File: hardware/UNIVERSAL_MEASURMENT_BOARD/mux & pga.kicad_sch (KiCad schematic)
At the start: 11 parts, among them U3 PGA280AIPW, U4 CD4097BM

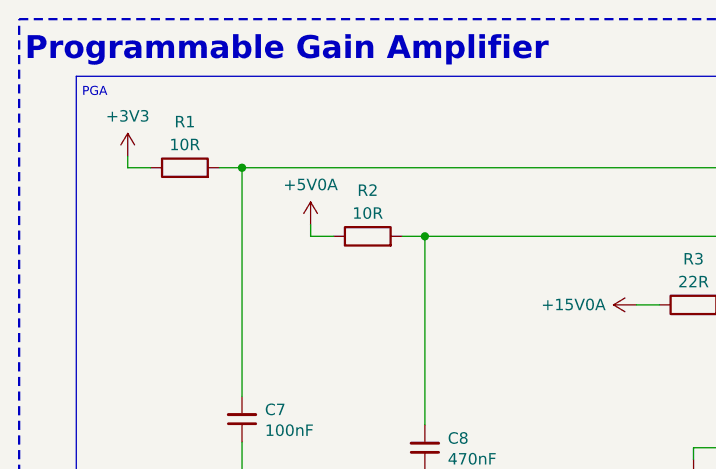
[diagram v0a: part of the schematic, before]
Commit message: Fixed VOUT range of PGA to 3.0V, fixed GPIO connection between FDCAN and MCU, added 1.5V VREF to PGA, changed value of enable divider of 7V DCDC converter.
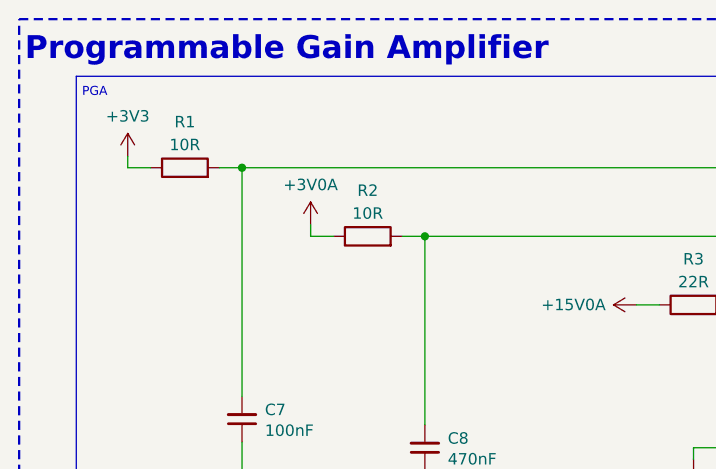
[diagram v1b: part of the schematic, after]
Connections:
- net +5V0A renamed +3V0A
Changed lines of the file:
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@@
 (kicad_sch
-	(version 20260101)
+	(version 20260306)
 	(generator "eeschema")
 	(generator_version "10.0")
@@
 		(title "Universal Measurment Board")
 		(date "2026-03-26")
-		(rev "1.9.21")
+		(rev "1.11.22")
 		(company "PUT Motorsport Formula Student Team")
 		(comment 1 "Designed by Marcin Trzmiel under")
@@
 			)
 		)
-		(property "Value" "+5V0A"
+		(property "Value" "+3V0A"
 			(at 53.975 40.005 0)
 			(show_name no)

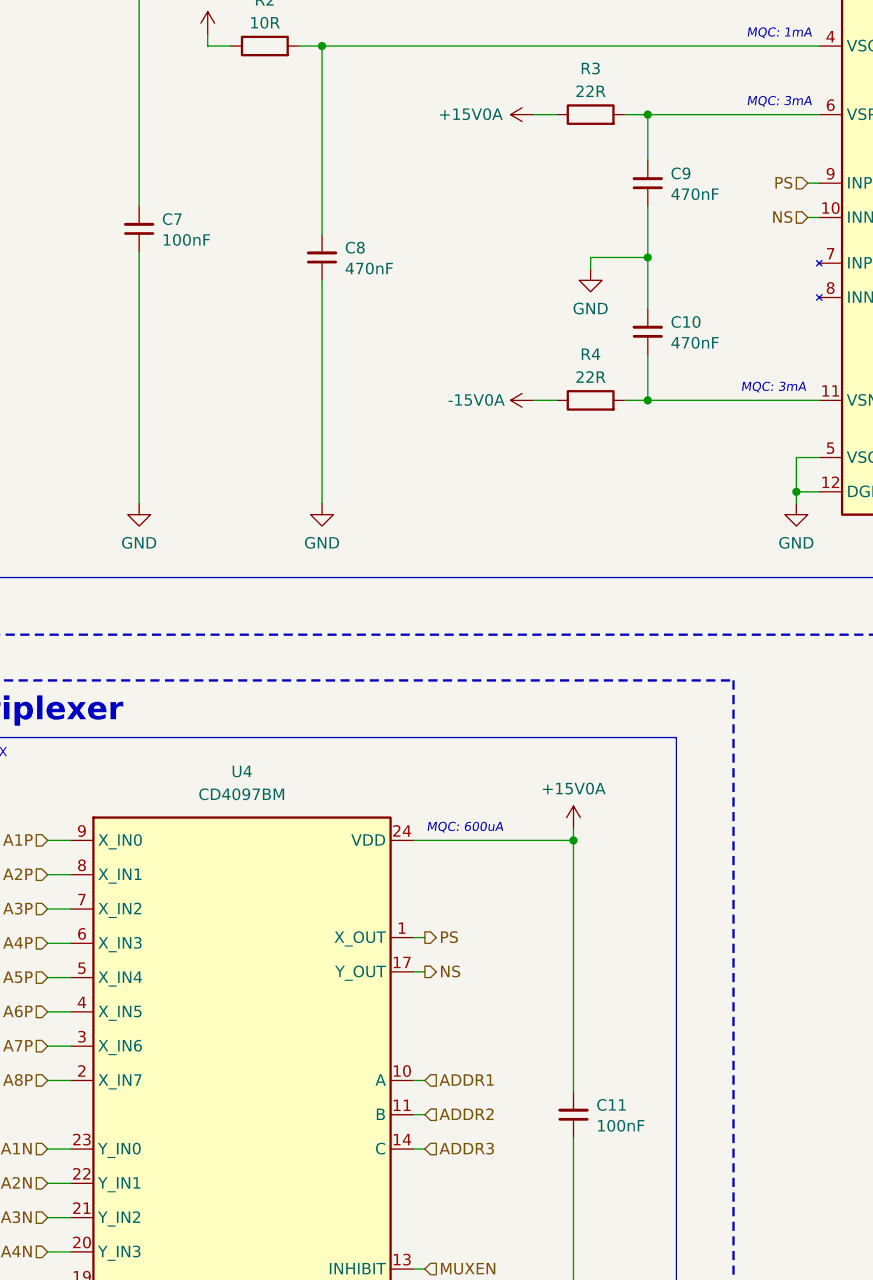
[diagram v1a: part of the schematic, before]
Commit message: Reduced PCB dimensions, working on power section
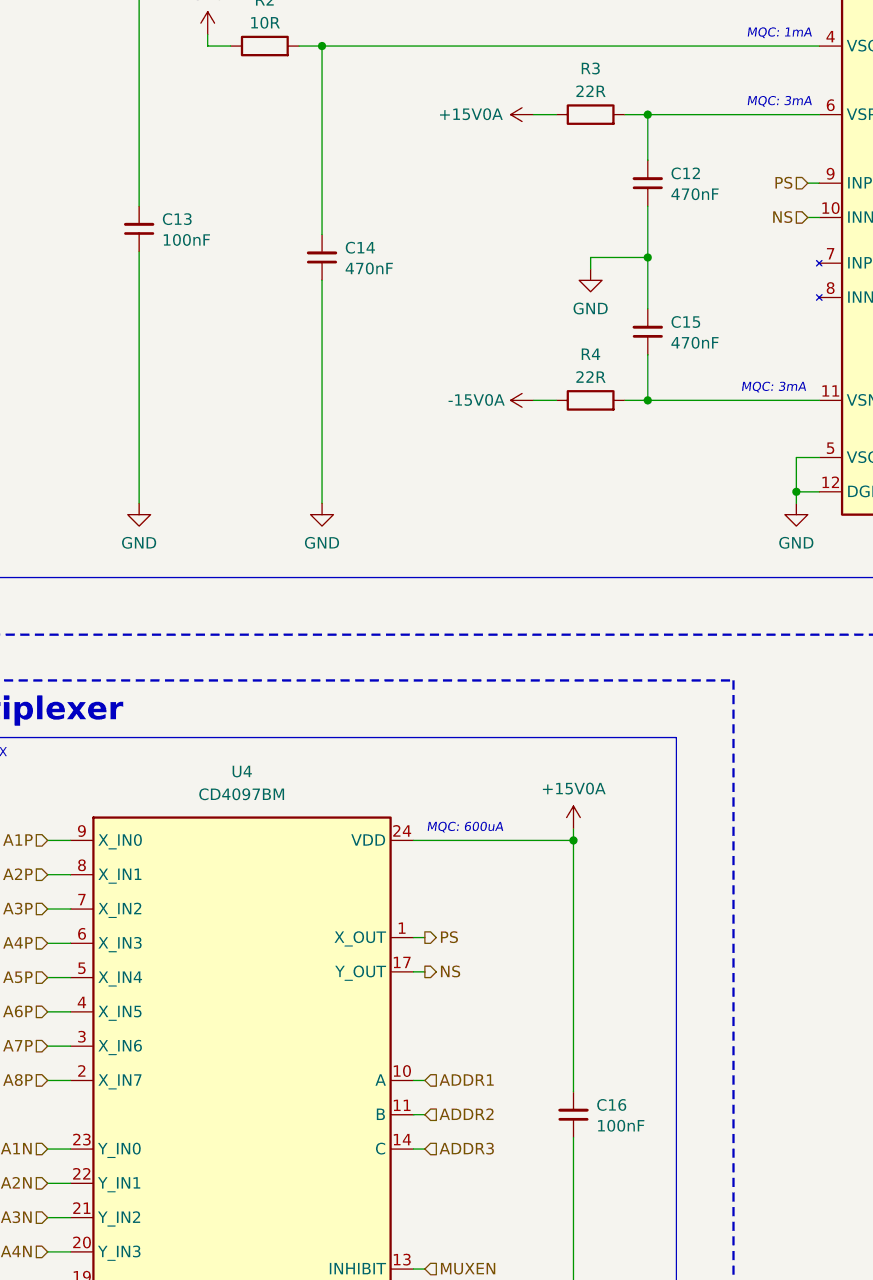
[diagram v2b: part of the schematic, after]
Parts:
- renumbered C9 to C12, C7 to C13, C8 to C14, C10 to C15, C11 to C16
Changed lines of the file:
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@@
 		(in_pos_files yes)
 		(dnp no)
-		(property "Reference" "#PWR024"
+		(property "Reference" "#PWR031"
 			(at 96.52 76.835 0)
 			(hide yes)
@@
 			(project "UNIVERSAL_MEASURMENT_BOARD"
 				(path "/92c00310-4384-4ef3-9368-efad75526047/2f9d6be2-539e-4cd2-829d-3839cc14b053"
-					(reference "#PWR024")
+					(reference "#PWR031")
 					(unit 1)
 				)
@@
 		(in_pos_files yes)
 		(dnp no)
-		(property "Reference" "#PWR022"
+		(property "Reference" "#PWR030"
 			(at 93.98 53.34 0)
 			(hide yes)
@@
 			(project "UNIVERSAL_MEASURMENT_BOARD"
 				(path "/92c00310-4384-4ef3-9368-efad75526047/2f9d6be2-539e-4cd2-829d-3839cc14b053"
-					(reference "#PWR022")
+					(reference "#PWR030")
 					(unit 1)
 				)
@@
 		(in_pos_files yes)
 		(dnp no)
-		(property "Reference" "C10"
+		(property "Reference" "C15"
 			(at 105.41 76.4286 0)
 			(show_name no)
@@
 			(project "UNIVERSAL_MEASURMENT_BOARD"
 				(path "/92c00310-4384-4ef3-9368-efad75526047/2f9d6be2-539e-4cd2-829d-3839cc14b053"
-					(reference "C10")
+					(reference "C15")
 					(unit 1)
 				)
@@
 		(in_pos_files yes)
 		(dnp no)
-		(property "Reference" "C8"
+		(property "Reference" "C14"
 			(at 69.215 68.1736 0)
 			(show_name no)
@@
 			(project "UNIVERSAL_MEASURMENT_BOARD"
 				(path "/92c00310-4384-4ef3-9368-efad75526047/2f9d6be2-539e-4cd2-829d-3839cc14b053"
-					(reference "C8")
+					(reference "C14")
 					(unit 1)
 				)
@@
 		(in_pos_files yes)
 		(dnp no)
-		(property "Reference" "#PWR021"
+		(property "Reference" "#PWR034"
 			(at 66.675 102.87 0)
 			(hide yes)
@@
 			(project "UNIVERSAL_MEASURMENT_BOARD"
 				(path "/92c00310-4384-4ef3-9368-efad75526047/2f9d6be2-539e-4cd2-829d-3839cc14b053"
-					(reference "#PWR021")
+					(reference "#PWR034")
 					(unit 1)
 				)
@@
 		(in_pos_files yes)
 		(dnp no)
-		(property "Reference" "#PWR029"
+		(property "Reference" "#PWR038"
 			(at 94.615 202.565 0)
 			(hide yes)
@@
 			(project "UNIVERSAL_MEASURMENT_BOARD"
 				(path "/92c00310-4384-4ef3-9368-efad75526047/2f9d6be2-539e-4cd2-829d-3839cc14b053"
-					(reference "#PWR029")
+					(reference "#PWR038")
 					(unit 1)
 				)
@@
 		(in_pos_files yes)
 		(dnp no)
-		(property "Reference" "#PWR028"
+		(property "Reference" "#PWR036"
 			(at 94.615 136.525 0)
 			(hide yes)
@@
 			(project "UNIVERSAL_MEASURMENT_BOARD"
 				(path "/92c00310-4384-4ef3-9368-efad75526047/2f9d6be2-539e-4cd2-829d-3839cc14b053"
-					(reference "#PWR028")
+					(reference "#PWR036")
 					(unit 1)
 				)
@@
 		(in_pos_files yes)
 		(dnp no)
-		(property "Reference" "C9"
+		(property "Reference" "C12"
 			(at 105.41 59.9186 0)
 			(show_name no)
@@
 			(project "UNIVERSAL_MEASURMENT_BOARD"
 				(path "/92c00310-4384-4ef3-9368-efad75526047/2f9d6be2-539e-4cd2-829d-3839cc14b053"
-					(reference "C9")
+					(reference "C12")
 					(unit 1)
 				)
@@
 		(in_pos_files yes)
 		(dnp no)
-		(property "Reference" "#PWR026"
+		(property "Reference" "#PWR028"
 			(at 175.26 44.45 0)
 			(hide yes)
@@
 			(project "UNIVERSAL_MEASURMENT_BOARD"
 				(path "/92c00310-4384-4ef3-9368-efad75526047/2f9d6be2-539e-4cd2-829d-3839cc14b053"
-					(reference "#PWR026")
+					(reference "#PWR028")
 					(unit 1)
 				)
@@
 		(in_pos_files yes)
 		(dnp no)
-		(property "Reference" "#PWR023"
+		(property "Reference" "#PWR032"
 			(at 93.98 85.09 0)
 			(hide yes)
@@
 			(project "UNIVERSAL_MEASURMENT_BOARD"
 				(path "/92c00310-4384-4ef3-9368-efad75526047/2f9d6be2-539e-4cd2-829d-3839cc14b053"
-					(reference "#PWR023")
+					(reference "#PWR032")
 					(unit 1)
 				)
@@
 		(in_pos_files yes)
 		(dnp no)
-		(property "Reference" "#PWR018"
+		(property "Reference" "#PWR027"
 			(at 33.655 40.64 0)
 			(hide yes)
@@
 			(project "UNIVERSAL_MEASURMENT_BOARD"
 				(path "/92c00310-4384-4ef3-9368-efad75526047/2f9d6be2-539e-4cd2-829d-3839cc14b053"
-					(reference "#PWR018")
+					(reference "#PWR027")
 					(unit 1)
 				)
@@
 		(in_pos_files yes)
 		(dnp no)
-		(property "Reference" "#PWR027"
+		(property "Reference" "#PWR037"
 			(at 79.375 202.565 0)
 			(hide yes)
@@
 			(project "UNIVERSAL_MEASURMENT_BOARD"
 				(path "/92c00310-4384-4ef3-9368-efad75526047/2f9d6be2-539e-4cd2-829d-3839cc14b053"
-					(reference "#PWR027")
+					(reference "#PWR037")
 					(unit 1)
 				)
@@
 		(in_pos_files yes)
 		(dnp no)
-		(property "Reference" "C11"
+		(property "Reference" "C16"
 			(at 97.155 163.4236 0)
 			(show_name no)
@@
 			(project "UNIVERSAL_MEASURMENT_BOARD"
 				(path "/92c00310-4384-4ef3-9368-efad75526047/2f9d6be2-539e-4cd2-829d-3839cc14b053"
-					(reference "C11")
+					(reference "C16")
 					(unit 1)
 				)
@@
 		(in_pos_files yes)
 		(dnp no)
-		(property "Reference" "C7"
+		(property "Reference" "C13"
 			(at 48.895 64.9986 0)
 			(show_name no)
@@
 			(project "UNIVERSAL_MEASURMENT_BOARD"
 				(path "/92c00310-4384-4ef3-9368-efad75526047/2f9d6be2-539e-4cd2-829d-3839cc14b053"
-					(reference "C7")
+					(reference "C13")
 					(unit 1)
 				)
@@
 		(in_pos_files yes)
 		(dnp no)
-		(property "Reference" "#PWR019"
+		(property "Reference" "#PWR033"
 			(at 46.355 102.87 0)
 			(hide yes)
@@
 			(project "UNIVERSAL_MEASURMENT_BOARD"
 				(path "/92c00310-4384-4ef3-9368-efad75526047/2f9d6be2-539e-4cd2-829d-3839cc14b053"
-					(reference "#PWR019")
+					(reference "#PWR033")
 					(unit 1)
 				)
@@
 		(in_pos_files yes)
 		(dnp no)
-		(property "Reference" "#PWR025"
+		(property "Reference" "#PWR035"
 			(at 119.38 102.87 0)
 			(hide yes)
@@
 			(project "UNIVERSAL_MEASURMENT_BOARD"
 				(path "/92c00310-4384-4ef3-9368-efad75526047/2f9d6be2-539e-4cd2-829d-3839cc14b053"
-					(reference "#PWR025")
+					(reference "#PWR035")
 					(unit 1)
 				)
@@
 		(in_pos_files yes)
 		(dnp no)
-		(property "Reference" "#PWR020"
+		(property "Reference" "#PWR029"
 			(at 53.975 48.26 0)
 			(hide yes)
@@
 			(project "UNIVERSAL_MEASURMENT_BOARD"
 				(path "/92c00310-4384-4ef3-9368-efad75526047/2f9d6be2-539e-4cd2-829d-3839cc14b053"
-					(reference "#PWR020")
+					(reference "#PWR029")
 					(unit 1)
 				)
